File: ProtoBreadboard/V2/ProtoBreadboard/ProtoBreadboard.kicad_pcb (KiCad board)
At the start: 2 copper layers, 180.3 x 167.6 mm, 63 parts, among them IC1 AT90USB1286-AU, IC2 BSS138, IC3 BSS138, J1 Conn_01x30_Female, J10 Conn_01x04_Female, J11 Conn_01x32_Female, J12 Conn_01x06_Female, J13 Conn_01x08_Female, J14 Conn_01x08_Female, J15 Conn_01x04_Female, J16 Conn_01x03_Female, J17 Conn_01x03_Female, J18 Conn_01x07_Female, J19 Conn_01x02_Female, J2 Conn_01x10_Female, J20 Conn_01x02_Female, J21 Conn_01x02_Female, J22 AVR-ISP-6, J23 Conn_01x02_Female, J24 Conn_01x03_Female, J25 Conn_01x07_Female, J26 Conn_01x03_Female, J27 Conn_02x03_Counter_Clockwise, J28 Conn_01x03_Female, J29 Conn_01x02_Female, J3 Conn_01x32_Female, J30 Conn_01x02_Female, J31 Conn_01x02_Female, J32 Conn_01x02_Female, J4 Conn_01x10_Female, J5 Conn_01x30_Female, J6 Conn_01x02_Female, J7 Conn_01x02_Female, J8 Conn_01x06_Female, J9 Conn_01x04_Female, SW1 RotaryEncoder_Switch, SW2 RotaryEncoder_Switch, U1 IS31FL3741A, U2 AP2112K-3.3, U3 PRTR5V0U2X, Y1 Crystal

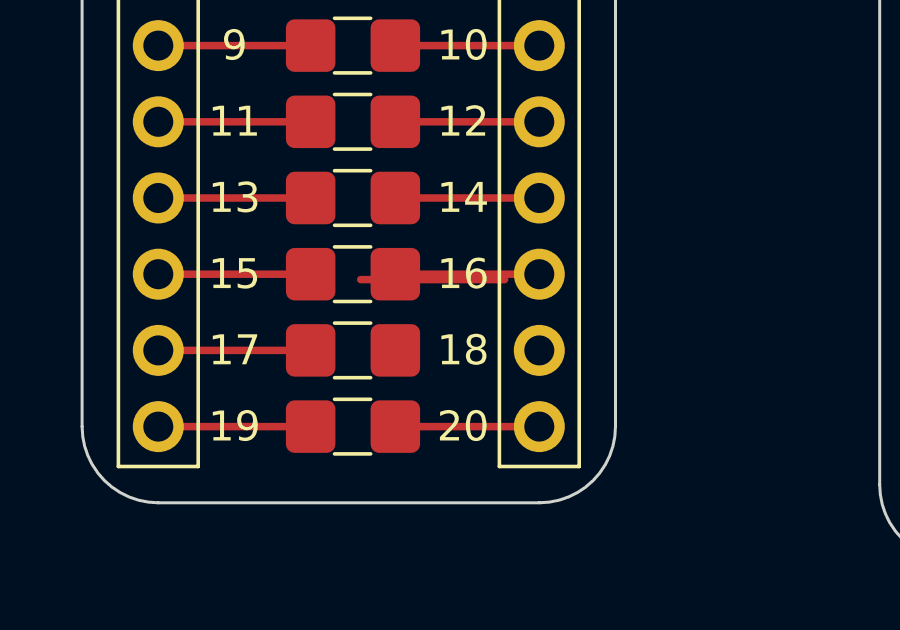
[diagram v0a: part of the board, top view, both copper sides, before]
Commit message: added oled adafruit link, removed useless csv
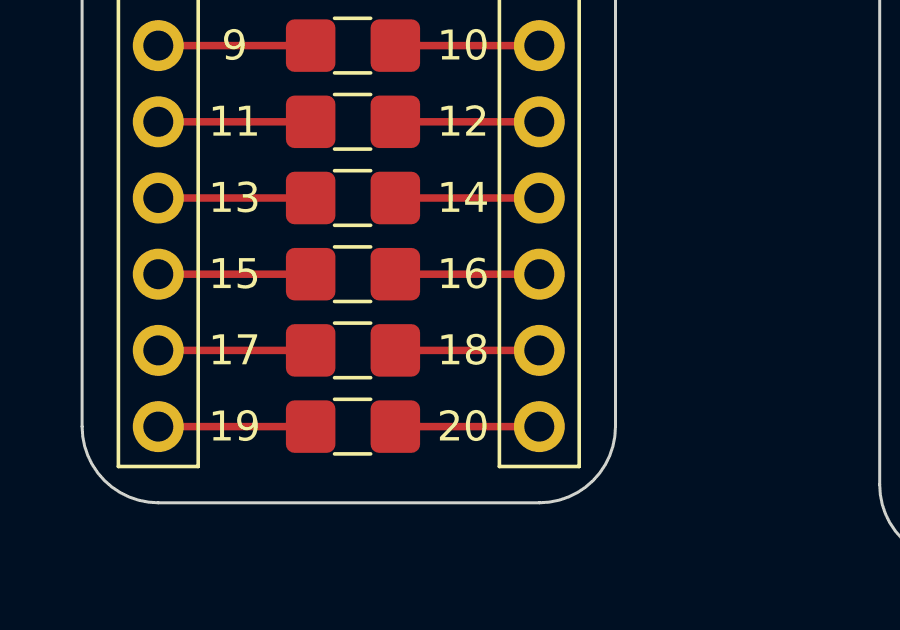
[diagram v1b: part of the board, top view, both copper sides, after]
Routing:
- net Net-(G9-Pad2): track 0.00 -> 4.80 mm
- net Net-(G8-Pad2): track 9.60 -> 4.80 mm
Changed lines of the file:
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@@
   (segment (start 24.21255 36.16) (end 19.38745 36.16) (width 0.25) (layer "F.Cu") (net 15))
   (segment (start 27.03485 36.16) (end 31.83345 36.16) (width 0.25) (layer "F.Cu") (net 16))
-  (segment (start 25.88025 36.34) (end 30.67885 36.34) (width 0.25) (layer "F.Cu") (net 16))
   (segment (start 19.38745 38.7) (end 24.21255 38.7) (width 0.25) (layer "F.Cu") (net 17))
+  (segment (start 27.03485 38.7) (end 31.83345 38.7) (width 0.25) (layer "F.Cu") (net 18))
   (segment (start 24.21255 41.24) (end 19.38745 41.24) (width 0.25) (layer "F.Cu") (net 19))
   (segment (start 27.03485 41.24) (end 31.83345 41.24) (width 0.25) (layer "F.Cu") (net 20))
